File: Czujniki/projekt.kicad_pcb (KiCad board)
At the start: 2 copper layers, 72.4 x 45.7 mm, 78 parts, among them P1 CONN_01X08, P2 CONN_01X06, P3 CONN_01X05, T1 Si2323DS, T2 FDV303N, T3 FDV303N, T4 Si2323DS, T5 Si2323DS, U1 MCP1700, U10 PCA9306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

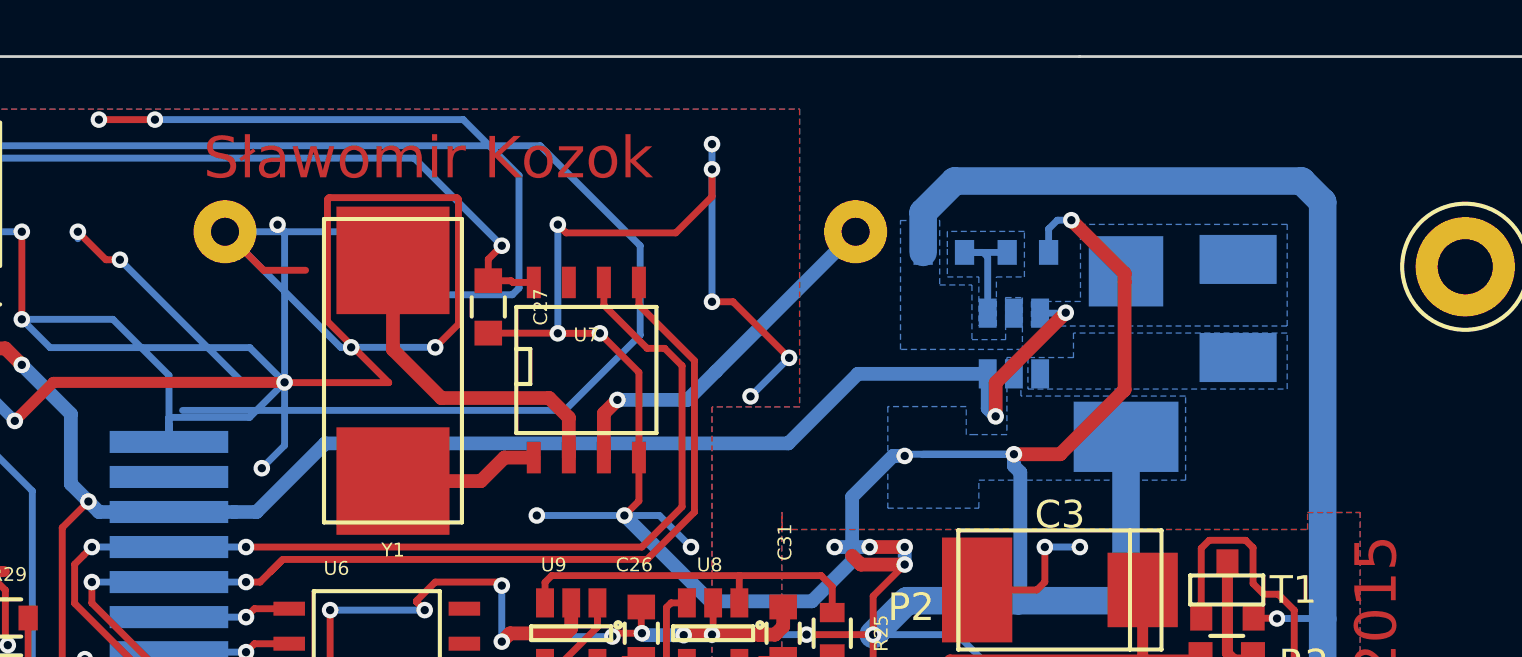
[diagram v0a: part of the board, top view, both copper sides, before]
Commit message: Changed switch placement (from main to sensor board)
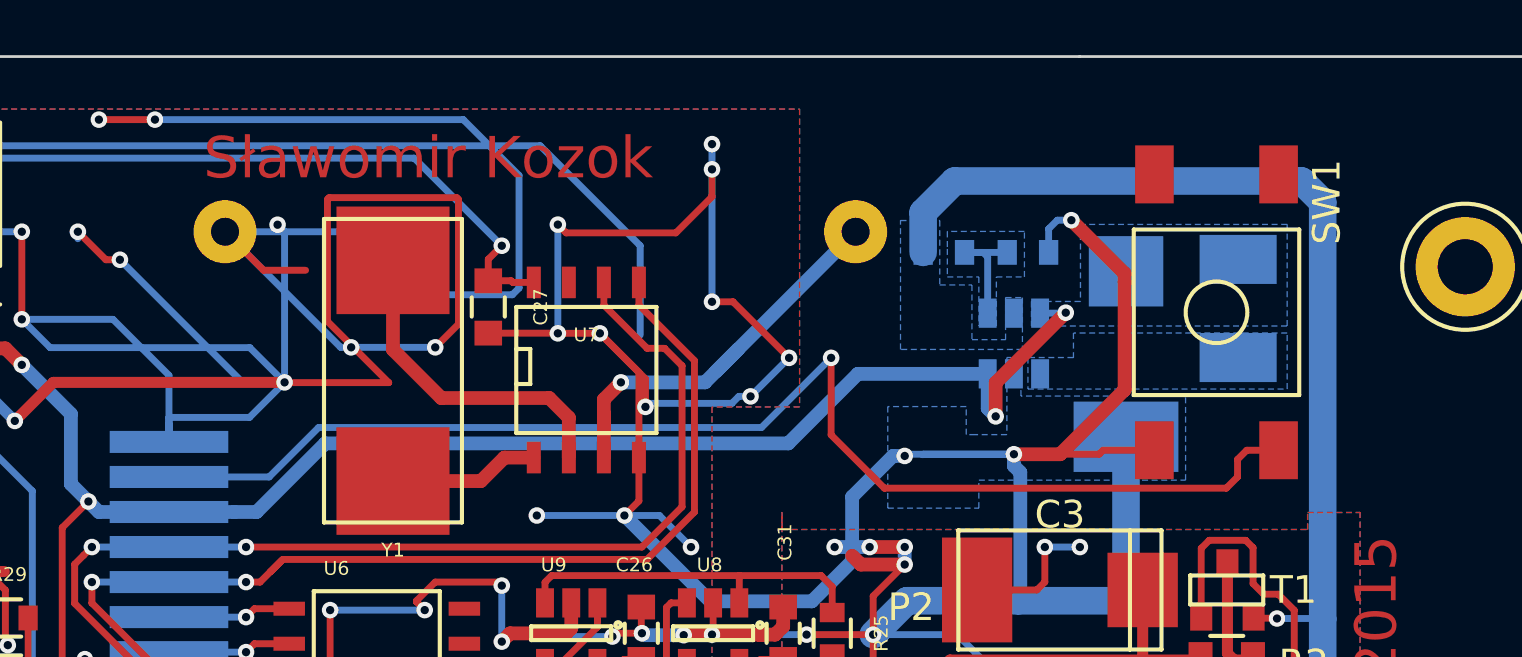
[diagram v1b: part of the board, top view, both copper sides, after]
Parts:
- added SW1: SW_PUSH_SMALL, Footprinty:TACT_SW_ONE_PAIR, F.Cu at (218.3, 64.5)
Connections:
- P1 pad 7: (no net) -> Net-(P1-Pad7)
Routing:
- net Net-(P1-Pad7): track 0.00 -> 46.5 mm, vias 0 -> 1
- net GND: track 806.8 -> 798.1 mm
- net Net-(BT1-Pad1): track 13.5 -> 15.4 mm
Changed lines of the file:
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@@
-(kicad_pcb (version 4) (host pcbnew no-vcs-found-product)
+(kicad_pcb (version 4) (host pcbnew 0.201507280910+6003~25~ubuntu14.04.1-product)
   (general
-    (links 172)
+    (links 174)
     (no_connects 0)
-    (area 143.146483 39.116106 260.73 113.825)
+    (area 157.429999 55.194999 229.920001 101.015001)
     (thickness 1.6)
     (drawings 13)
-    (tracks 1168)
+    (tracks 1189)
     (zones 0)
-    (modules 78)
-    (nets 47)
+    (modules 79)
+    (nets 48)
   )
   (page A4)
@@
   (net 45 "Net-(DET1-PadA)")
   (net 46 "Net-(DET1-PadH1)")
+  (net 47 "Net-(P1-Pad7)")
   (net_class Default "To jest domyślna klasa połączeń."
     (clearance 0.2)
@@
     (add_net "Net-(DET1-PadH1)")
     (add_net "Net-(L1-Pad2)")
+    (add_net "Net-(P1-Pad7)")
     (add_net "Net-(P2-Pad3)")
     (add_net "Net-(P2-Pad6)")
@@
     (pad 6 smd rect (at 6.35 0 90) (size 0.8 4.3) (layers B.Cu B.Paste B.Mask)
       (net 25 MAIN_VOL))
-    (pad 7 smd rect (at 7.62 0 90) (size 0.8 4.3) (layers B.Cu B.Paste B.Mask))
+    (pad 7 smd rect (at 7.62 0 90) (size 0.8 4.3) (layers B.Cu B.Paste B.Mask)
+      (net 47 "Net-(P1-Pad7)"))
     (pad 8 smd rect (at 8.89 0 90) (size 0.8 4.3) (layers B.Cu B.Paste B.Mask)
       (net 1 GND))
@@
     (pad 1 thru_hole circle (at 0 0) (size 3.6 3.6) (drill 2) (layers *.Cu *.Mask F.SilkS))
   )
+  (module Footprinty:TACT_SW_ONE_PAIR (layer F.Cu)
+    (at 218.313 64.516 90)
+    (fp_text reference SW1 (at 4 4 90) (layer F.SilkS)
+      (effects (font (size 1 1) (thickness 0.15)))
+    )
+    (fp_text value SW_PUSH_SMALL (at -3 -4 90) (layer F.Fab)
+      (effects (font (size 1 1) (thickness 0.15)))
+    )
+    (fp_circle (center 0 0) (end 0.5 1) (layer F.SilkS) (width 0.15))
+    (fp_line (start -3 -3) (end 3 -3) (layer F.SilkS) (width 0.15))
+    (fp_line (start 3 -3) (end 3 3) (layer F.SilkS) (width 0.15))
+    (fp_line (start 3 3) (end -3 3) (layer F.SilkS) (width 0.15))
+    (fp_line (start -3 3) (end -3 -3) (layer F.SilkS) (width 0.15))
+    (pad 1 smd rect (at -5 -2.25 90) (size 2.1 1.4) (layers F.Cu F.Paste F.Mask)
+      (net 1 GND))
+    (pad "" smd rect (at 5 -2.25 90) (size 2.1 1.4) (layers F.Cu F.Paste F.Mask))
+    (pad 2 smd rect (at -5 2.25 90) (size 2.1 1.4) (layers F.Cu F.Paste F.Mask)
+      (net 47 "Net-(P1-Pad7)"))
+    (pad "" smd rect (at 5 2.25 90) (size 2.1 1.4) (layers F.Cu F.Paste F.Mask))
+  )
   (dimension 72.39 (width 0.3) (layer Cmts.User)
     (gr_text "72,390 mm" (at 193.675 112.474999) (layer Cmts.User)
@@
   (gr_line (start 213.36 55.245) (end 157.48 55.245) (angle 90) (layer Edge.Cuts) (width 0.1))
   (gr_line (start 157.48 100.965) (end 213.36 100.965) (angle 90) (layer Edge.Cuts) (width 0.1))
+  (segment (start 214.202 69.516) (end 214.057413 69.660587) (width 0.25) (layer F.Cu) (net 1))
+  (segment (start 214.057413 69.660587) (end 210.968701 69.660587) (width 0.25) (layer F.Cu) (net 1))
+  (segment (start 216.063 69.516) (end 214.202 69.516) (width 0.25) (layer F.Cu) (net 1))
+  (segment (start 197.612 67.945) (end 197.612 66.929) (width 0.25) (layer F.Cu) (net 1))
+  (segment (start 197.612 66.929) (end 195.961 65.278) (width 0.25) (layer F.Cu) (net 1))
+  (segment (start 200.743736 67.818) (end 197.739 67.818) (width 0.25) (layer B.Cu) (net 1))
+  (segment (start 197.739 67.818) (end 197.612 67.945) (width 0.25) (layer B.Cu) (net 1))
+  (via (at 197.612 67.945) (size 0.6) (drill 0.3) (layers F.Cu B.Cu) (net 1))
+  (segment (start 201.422 67.564) (end 200.997736 67.564) (width 0.25) (layer B.Cu) (net 1))
+  (segment (start 200.997736 67.564) (end 200.743736 67.818) (width 0.25) (layer B.Cu) (net 1))
   (segment (start 212.09 73.025) (end 213.36 73.025) (width 0.25) (layer B.Cu) (net 1))
   (via (at 213.36 73.025) (size 0.6) (drill 0.3) (layers F.Cu B.Cu) (net 1))
@@
   (segment (start 212.645101 69.660587) (end 214.981901 67.323787) (width 0.5) (layer F.Cu) (net 1))
   (segment (start 210.968701 69.660587) (end 212.645101 69.660587) (width 0.5) (layer F.Cu) (net 1))
-  (segment (start 184.531 67.056) (end 184.531 69.342) (width 0.25) (layer B.Cu) (net 1))
-  (segment (start 184.531 69.342) (end 183.7055 70.1675) (width 0.25) (layer B.Cu) (net 1))
-  (via (at 183.7055 70.1675) (size 0.6) (drill 0.3) (layers F.Cu B.Cu) (net 1))
   (segment (start 198.628 89.3445) (end 198.250741 89.721759) (width 0.25) (layer B.Cu) (net 1))
   (segment (start 198.250741 89.721759) (end 198.250741 92.246521) (width 0.25) (layer B.Cu) (net 1))
@@
   (segment (start 166.5605 59.1185) (end 167.20101 58.47799) (width 0.25) (layer B.Cu) (net 1))
   (segment (start 167.20101 58.47799) (end 193.79649 58.47799) (width 0.25) (layer B.Cu) (net 1))
-  (segment (start 197.4215 65.3415) (end 194.691 68.072) (width 0.25) (layer B.Cu) (net 1))
   (segment (start 193.79649 58.47799) (end 197.4215 62.103) (width 0.25) (layer B.Cu) (net 1))
   (segment (start 197.4215 62.103) (end 197.4215 65.3415) (width 0.25) (layer B.Cu) (net 1))
-  (segment (start 194.691 68.072) (end 180.833 68.072) (width 0.25) (layer B.Cu) (net 1))
   (segment (start 180.34 68.565) (end 180.34 69.215) (width 0.25) (layer B.Cu) (net 1))
   (segment (start 169.672 58.801) (end 166.878 58.801) (width 0.25) (layer F.Cu) (net 1))
@@
   (segment (start 212.226701 61.493787) (end 212.543501 61.176987) (width 0.25) (layer B.Cu) (net 1))
   (segment (start 207.684481 69.660587) (end 207.666701 69.678367) (width 0.25) (layer B.Cu) (net 1))
-  (segment (start 196.596 67.691) (end 199.136 67.691) (width 0.5) (layer B.Cu) (net 2))
-  (segment (start 199.136 67.691) (end 200.170429 66.656571) (width 0.5) (layer B.Cu) (net 2))
-  (segment (start 200.170429 66.656571) (end 205.232 61.595) (width 0.5) (layer B.Cu) (net 2))
-  (segment (start 196.105411 69.782679) (end 196.105411 68.181589) (width 0.5) (layer F.Cu) (net 2))
-  (segment (start 196.105411 68.181589) (end 196.596 67.691) (width 0.5) (layer F.Cu) (net 2))
-  (via (at 196.596 67.691) (size 0.6) (drill 0.3) (layers F.Cu B.Cu) (net 2))
+  (segment (start 200.170429 66.656571) (end 200.960922 65.866078) (width 0.5) (layer B.Cu) (net 2))
+  (segment (start 196.723 67.056) (end 199.771 67.056) (width 0.5) (layer B.Cu) (net 2))
+  (segment (start 200.960922 65.866078) (end 205.232 61.595) (width 0.5) (layer B.Cu) (net 2))
+  (segment (start 199.771 67.056) (end 200.960922 65.866078) (width 0.5) (layer B.Cu) (net 2))
+  (via (at 196.723 67.056) (size 0.6) (drill 0.3) (layers F.Cu B.Cu) (net 2))
+  (segment (start 196.105411 68.737809) (end 196.105411 68.181589) (width 0.5) (layer F.Cu) (net 2))
+  (segment (start 196.105411 69.782679) (end 196.105411 68.737809) (width 0.5) (layer F.Cu) (net 2))
+  (segment (start 196.105411 68.737809) (end 196.105411 67.673589) (width 0.5) (layer F.Cu) (net 2))
+  (segment (start 196.105411 67.673589) (end 196.723 67.056) (width 0.5) (layer F.Cu) (net 2))
   (segment (start 175.387 78.980483) (end 175.387 70.993) (width 0.25) (layer B.Cu) (net 3))
   (segment (start 175.387 70.993) (end 170.167643 65.773643) (width 0.25) (layer B.Cu) (net 3))
@@
   (segment (start 184.15 95.885) (end 184.15 94.107) (width 0.25) (layer B.Cu) (net 46))
   (segment (start 197.04674 97.40352) (end 185.66852 97.40352) (width 0.25) (layer B.Cu) (net 46))
+  (segment (start 204.343 66.167) (end 204.343 68.961) (width 0.25) (layer F.Cu) (net 47))
+  (segment (start 219.409 69.516) (end 220.563 69.516) (width 0.25) (layer F.Cu) (net 47))
+  (segment (start 204.343 68.961) (end 206.273001 70.891001) (width 0.25) (layer F.Cu) (net 47))
+  (segment (start 206.273001 70.891001) (end 218.668999 70.891001) (width 0.25) (layer F.Cu) (net 47))
+  (segment (start 218.668999 70.891001) (end 219.075 70.485) (width 0.25) (layer F.Cu) (net 47))
+  (segment (start 219.075 70.485) (end 219.075 69.85) (width 0.25) (layer F.Cu) (net 47))
+  (segment (start 219.075 69.85) (end 219.409 69.516) (width 0.25) (layer F.Cu) (net 47))
+  (segment (start 197.993 68.692415) (end 201.817585 68.692415) (width 0.25) (layer B.Cu) (net 47))
+  (segment (start 201.817585 68.692415) (end 204.343 66.167) (width 0.25) (layer B.Cu) (net 47))
+  (via (at 204.343 66.167) (size 0.6) (drill 0.3) (layers F.Cu B.Cu) (net 47))
+  (segment (start 185.764399 68.692415) (end 197.993 68.692415) (width 0.25) (layer B.Cu) (net 47))
+  (segment (start 183.971814 70.485) (end 185.764399 68.692415) (width 0.25) (layer B.Cu) (net 47))
+  (segment (start 180.34 70.485) (end 183.971814 70.485) (width 0.25) (layer B.Cu) (net 47))
   (zone (net 25) (net_name MAIN_VOL) (layer B.Cu) (hatch edge 0.508)
     (connect_pads yes (clearance 0.25))
